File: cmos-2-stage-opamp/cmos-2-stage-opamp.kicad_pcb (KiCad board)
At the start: 2 copper layers, 39 x 34.5 mm, 35 parts, among them J1 Conn_01x05, Q1 DMN62DOU, Q2 DMN62DOU, Q3 DMN2004DMK-7, Q4 DMP2240UDM-7, Q5 DMN62DOU, Q8 DMP510DL, Q9 DMN62DOU

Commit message: cleanup: added annotations for tp + board images
DRC passed
Ready to submit to OSHPark
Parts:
- moved Q4 2.57 mm to (144.5, 61.8)
- renumbered TP1 to TP1VDD, TP2 to TP2Out, TP3 to TP3Bias, TP4 to TP4Bias, TP5 to TP5VSS, TP6 to TP6Tail, TP7 to TP7Mirror
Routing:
- net Net-(C1-Pad1): track 67.0 -> 70.9 mm
- net VDD: track 63.4 -> 66.9 mm
- net Net-(Q4A-DN): track 4.66 -> 8.11 mm
- net Net-(Q4B-SP): track 4.29 -> 7.31 mm
- net /mirror: track 25.6 -> 27.9 mm
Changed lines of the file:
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@@
 		)
 		(fp_text user "${REFERENCE}"
-			(at -4.445 4 360)
+			(at -4.445 4 0)
 			(layer "F.Fab")
 			(effects
@@
 		)
 		(fp_text user "${REFERENCE}"
-			(at 0 0 360)
+			(at 0 0 0)
 			(layer "F.Fab")
 			(effects
@@
 		(descr "SMD rectangular pad as test Point, square 1.5mm side length")
 		(tags "test point SMD pad rectangle square")
-		(property "Reference" "TP7"
+		(property "Reference" "TP7Mirror"
 			(at 0 -1.648 0)
 			(layer "F.SilkS")
@@
 	(footprint "Package_TO_SOT_SMD:SOT-363_SC-70-6_Handsoldering"
 		(layer "F.Cu")
-		(at 142.7 63.5875)
+		(at 144.52 61.77)
 		(descr "SOT-363, SC-70-6, Handsoldering")
 		(tags "SOT-363 SC-70-6 Handsoldering")
@@
 		(descr "SMD rectangular pad as test Point, square 1.5mm side length")
 		(tags "test point SMD pad rectangle square")
-		(property "Reference" "TP6"
-			(at 0 -1.648 0)
+		(property "Reference" "TP6Tail"
+			(at -0.15 1.91 0)
 			(layer "F.SilkS")
 			(effects
@@
 		(descr "SMD rectangular pad as test Point, square 1.5mm side length")
 		(tags "test point SMD pad rectangle square")
-		(property "Reference" "TP2"
+		(property "Reference" "TP2Out"
 			(at 0 1.648 0)
 			(layer "B.SilkS")
@@
 		(descr "SMD rectangular pad as test Point, square 1.5mm side length")
 		(tags "test point SMD pad rectangle square")
-		(property "Reference" "TP3"
-			(at 0 1.648 0)
+		(property "Reference" "TP3Bias"
+			(at -0.14 1.56 0)
 			(layer "B.SilkS")
 			(effects
@@
 		(descr "SMD rectangular pad as test Point, square 1.5mm side length")
 		(tags "test point SMD pad rectangle square")
-		(property "Reference" "TP1"
+		(property "Reference" "TP1VDD"
 			(at 0 1.648 0)
 			(layer "B.SilkS")
@@
 		(descr "SMD rectangular pad as test Point, square 1.5mm side length")
 		(tags "test point SMD pad rectangle square")
-		(property "Reference" "TP5"
+		(property "Reference" "TP5VSS"
 			(at -0.16 1.82 0)
 			(layer "B.SilkS")
 			(effects
 				(font
-					(size 1 1)
+					(size 0.8 0.8)
 					(thickness 0.15)
 				)
@@
 		(descr "SMD rectangular pad as test Point, square 1.5mm side length")
 		(tags "test point SMD pad rectangle square")
-		(property "Reference" "TP4"
-			(at 0 1.66 0)
+		(property "Reference" "TP4Bias"
+			(at 0.3 1.58 0)
 			(layer "B.SilkS")
 			(effects
 				(font
-					(size 1 1)
-					(thickness 0.15)
+					(size 0.65 0.65)
+					(thickness 0.125)
 				)
 				(justify mirror)
@@
 	)
 	(segment
-		(start 138.15 70.79)
-		(end 137.331151 71.608849)
+		(start 149.42 51.25)
+		(end 149.42 68.52)
 		(width 0.2)
 		(layer "F.Cu")
@@
 	)
 	(segment
-		(start 146.55 48.38)
-		(end 146.55 68.695685)
+		(start 131.253129 60.236871)
+		(end 134.913129 60.236871)
 		(width 0.2)
 		(layer "F.Cu")
@@
 	)
 	(segment
-		(start 144.225685 71.02)
-		(end 140.708529 71.02)
+		(start 137.37 57.78)
+		(end 137.21 57.62)
 		(width 0.2)
 		(layer "F.Cu")
@@
 	)
 	(segment
-		(start 131.253129 60.236871)
-		(end 134.913129 60.236871)
+		(start 146.92 71.02)
+		(end 140.708529 71.02)
 		(width 0.2)
 		(layer "F.Cu")
@@
 	)
 	(segment
-		(start 137.37 57.78)
-		(end 137.21 57.62)
-		(width 0.2)
-		(layer "F.Cu")
-		(net 2)
-	)
-	(segment
 		(start 137.331151 71.608849)
 		(end 137.331151 71.75)
@@
 	)
 	(segment
-		(start 140.708529 71.02)
-		(end 140.478529 70.79)
+		(start 146.55 48.38)
+		(end 149.42 51.25)
 		(width 0.2)
 		(layer "F.Cu")
@@
 	)
 	(segment
+		(start 149.42 68.52)
+		(end 146.92 71.02)
+		(width 0.2)
+		(layer "F.Cu")
+		(net 2)
+	)
+	(segment
+		(start 138.15 70.79)
+		(end 137.331151 71.608849)
+		(width 0.2)
+		(layer "F.Cu")
+		(net 2)
+	)
+	(segment
 		(start 129.04 59.35)
 		(end 130.59 60.9)
@@
 	)
 	(segment
-		(start 146.55 68.695685)
-		(end 144.225685 71.02)
+		(start 140.708529 71.02)
+		(end 140.478529 70.79)
 		(width 0.2)
 		(layer "F.Cu")
@@
 	)
 	(segment
+		(start 148.5 68.64)
+		(end 148.5 53.44)
+		(width 0.2)
+		(layer "F.Cu")
+		(net 3)
+	)
+	(segment
 		(start 141.7125 68.5325)
 		(end 141.2575 68.5325)
@@
 	)
 	(segment
-		(start 144.39 68.615)
-		(end 146.04 68.64)
+		(start 148.5 53.44)
+		(end 145.63 50.57)
 		(width 0.2)
 		(layer "F.Cu")
@@
 	)
 	(segment
-		(start 145.54 50.48)
-		(end 145.63 50.57)
+		(start 144.39 68.615)
+		(end 148.5 68.64)
 		(width 0.2)
 		(layer "F.Cu")
@@
 	)
 	(segment
-		(start 146.04 68.64)
-		(end 146.04 50.98)
+		(start 145.54 50.48)
+		(end 145.63 50.57)
 		(width 0.2)
 		(layer "F.Cu")
@@
 	)
 	(segment
-		(start 146.04 50.98)
-		(end 145.63 50.57)
-		(width 0.2)
-		(layer "F.Cu")
-		(net 3)
-	)
-	(segment
 		(start 141.7125 68.5325)
 		(end 144.3075 68.5325)
@@
 	)
 	(segment
+		(start 142.14 62.37)
+		(end 142.19 62.42)
+		(width 0.2)
+		(layer "F.Cu")
+		(net 11)
+	)
+	(segment
 		(start 138.91 68.58)
 		(end 140.83 66.66)
@@
 	)
 	(segment
-		(start 140.620001 62.9375)
-		(end 140.32 63.237501)
+		(start 125.46 67.878456)
+		(end 126.161544 68.58)
 		(width 0.2)
 		(layer "F.Cu")
@@
 	)
 	(segment
-		(start 141.37 62.9375)
-		(end 144.03 62.9375)
+		(start 141.971815 62.42)
+		(end 140.83 63.561815)
 		(width 0.2)
 		(layer "F.Cu")
@@
 	)
 	(segment
-		(start 140.83 64.7775)
-		(end 141.37 64.2375)
+		(start 142.440001 61.12)
+		(end 142.14 61.420001)
 		(width 0.2)
 		(layer "F.Cu")
@@
 	)
 	(segment
-		(start 141.37 62.9375)
-		(end 140.620001 62.9375)
+		(start 142.14 61.420001)
+		(end 142.14 62.37)
 		(width 0.2)
 		(layer "F.Cu")
@@
 	)
 	(segment
-		(start 125.46 67.878456)
-		(end 126.161544 68.58)
+		(start 140.83 63.561815)
+		(end 140.83 64.7775)
 		(width 0.2)
 		(layer "F.Cu")
@@
 	)
 	(segment
-		(start 140.32 63.237501)
-		(end 140.32 64.12)
+		(start 142.19 62.42)
+		(end 143.19 62.42)
+		(width 0.2)
+		(layer "F.Cu")
+		(net 11)
+	)
+	(segment
+		(start 142.19 62.42)
+		(end 141.971815 62.42)
 		(width 0.2)
 		(layer "F.Cu")
@@
 	)
 	(segment
-		(start 131.42 68.58)
-		(end 138.91 68.58)
+		(start 143.19 61.12)
+		(end 145.85 61.12)
 		(width 0.2)
 		(layer "F.Cu")
@@
 	)
 	(segment
-		(start 140.4375 64.2375)
-		(end 141.37 64.2375)
+		(start 131.42 68.58)
+		(end 138.91 68.58)
 		(width 0.2)
 		(layer "F.Cu")
@@
 	)
 	(segment
-		(start 140.32 64.12)
-		(end 140.4375 64.2375)
+		(start 143.19 61.12)
+		(end 142.440001 61.12)
 		(width 0.2)
 		(layer "F.Cu")
@@
 	)
 	(segment
-		(start 145.1725 64.2375)
-		(end 145.42 63.99)
+		(start 126.76 69.87)
+		(end 127.28 70.39)
 		(width 0.2)
 		(layer "F.Cu")
@@
 	)
 	(segment
-		(start 144.03 64.2375)
-		(end 145.1725 64.2375)
+		(start 145.43 63.98)
+		(end 145.44 63.98)
 		(width 0.2)
 		(layer "F.Cu")
@@
 	)
 	(segment
-		(start 126.76 69.87)
-		(end 127.28 70.39)
+		(start 145.85 62.42)
+		(end 145.85 63.57)
 		(width 0.2)
 		(layer "F.Cu")
@@
 	)
 	(segment
-		(start 145.43 63.98)
-		(end 145.44 63.98)
+		(start 145.42 63.99)
+		(end 145.43 63.98)
 		(width 0.2)
 		(layer "F.Cu")
@@
 	)
 	(segment
-		(start 145.42 63.99)
-		(end 145.43 63.98)
+		(start 145.85 63.57)
+		(end 145.44 63.98)
 		(width 0.2)
 		(layer "F.Cu")
@@
 	)
 	(segment
-		(start 142.42 63.887501)
-		(end 142.42 66)
+		(start 143.19 61.77)
+		(end 143.939999 61.77)
 		(width 0.2)
 		(layer "F.Cu")
@@
 	)
 	(segment
-		(start 142.119999 63.5875)
-		(end 142.42 63.887501)
+		(start 144.24 62.070001)
+		(end 144.24 62.688456)
+		(width 0.2)
+		(layer "F.Cu")
+		(net 15)
+	)
+	(segment
+		(start 144.24 62.688456)
+		(end 143.740956 63.1875)
+		(width 0.2)
+		(layer "F.Cu")
+		(net 15)
+	)
+	(segment
+		(start 142.42 63.74)
+		(end 142.42 66)
 		(width 0.2)
 		(layer "F.Cu")
@@
 	)
 	(segment
-		(start 141.37 63.5875)
-		(end 142.119999 63.5875)
+		(start 143.740956 63.1875)
+		(end 142.9725 63.1875)
 		(width 0.2)
 		(layer "F.Cu")
@@
 	)
 	(segment
+		(start 142.9725 63.1875)
+		(end 142.42 63.74)
+		(width 0.2)
+		(layer "F.Cu")
+		(net 15)
+	)
+	(segment
+		(start 143.939999 61.77)
+		(end 144.24 62.070001)
+		(width 0.2)
+		(layer "F.Cu")
+		(net 15)
+	)
+	(segment
+		(start 145.158456 61.77)
+		(end 144.78 62.148456)
+		(width 0.2)
+		(layer "F.Cu")
+		(net 16)
+	)
+	(segment
+		(start 144.78 63.61)
+		(end 144.0525 63.61)
+		(width 0.2)
+		(layer "F.Cu")
+		(net 16)
+	)
+	(segment
+		(start 144.0525 63.61)
+		(end 144.03 63.5875)
+		(width 0.2)
+		(layer "F.Cu")
+		(net 16)
+	)
+	(segment
+		(start 144.78 62.148456)
+		(end 144.78 63.61)
+		(width 0.2)
+		(layer "F.Cu")
+		(net 16)
+	)
+	(segment
 		(start 142.98 63.887501)
 		(end 142.98 65.38)
@@
 		(width 0.2)
 		(layer "F.Cu")
+		(net 16)
+	)
+	(segment
+		(start 145.85 61.77)
+		(end 145.158456 61.77)
+		(width 0.2)
+		(layer "F.Cu")

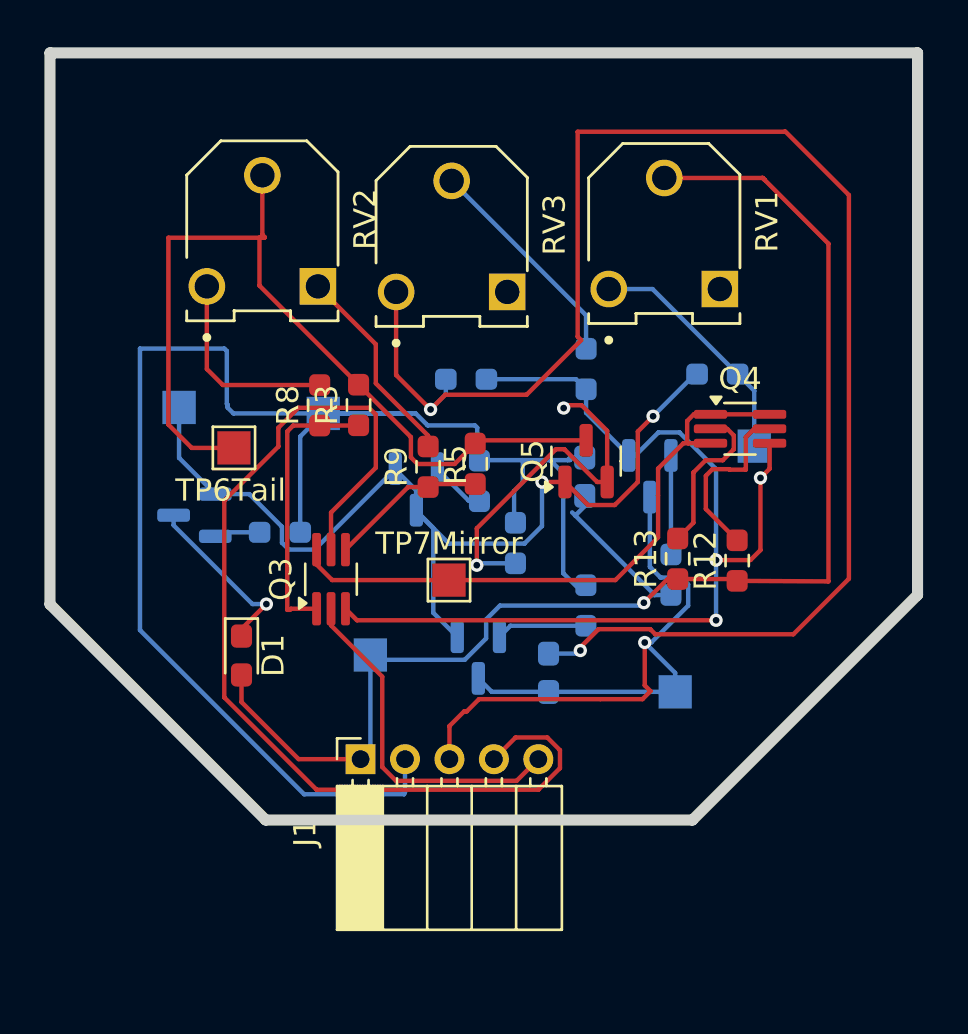
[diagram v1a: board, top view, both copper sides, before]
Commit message: final update on board
added senior design and date approved to chip using silkscreen.
added name of chip 2 stage cmos op-amp.
updated footprint of chip from 2.00 1*05 pin conn to 2.54 1*05 pin conn.
ran DRC and everything checks out perfectly.
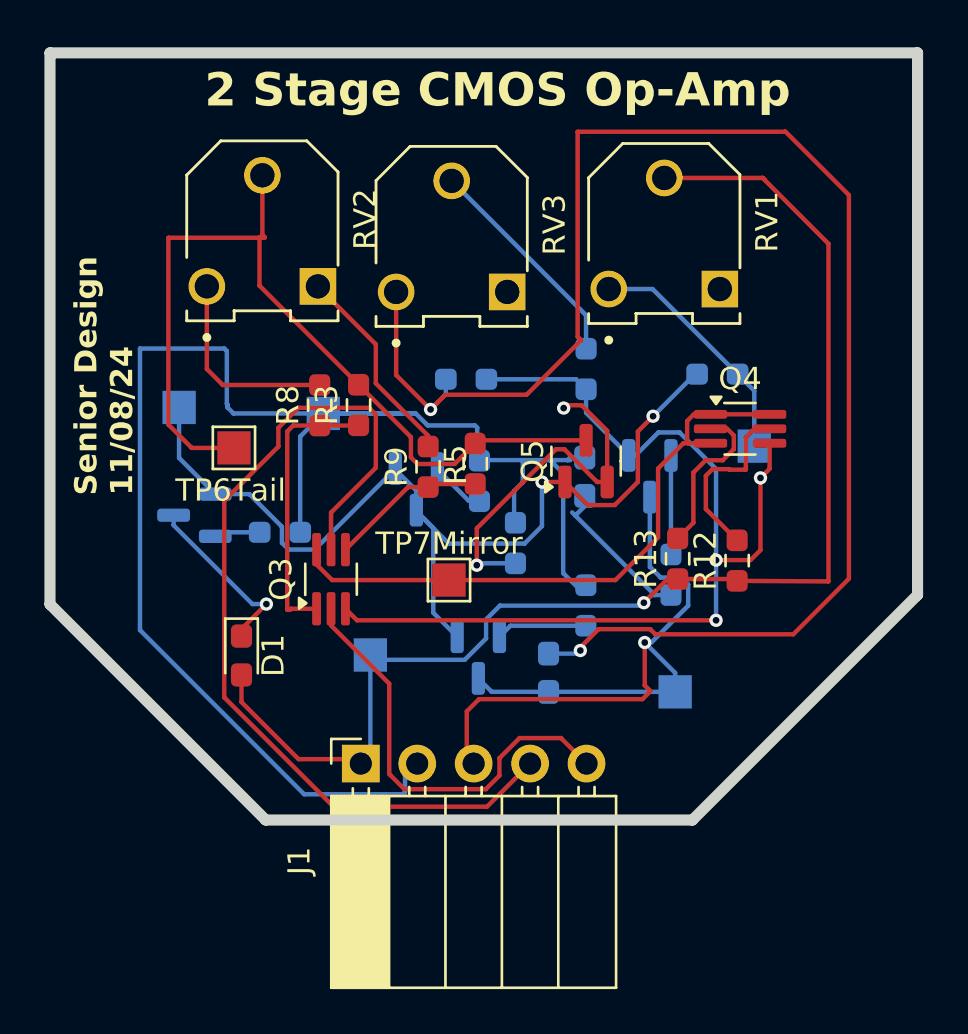
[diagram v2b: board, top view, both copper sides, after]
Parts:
- J1: footprint Connector_PinSocket_2.00mm:PinSocket_1x05_P2.00mm_Horizontal -> Connector_PinSocket_2.54mm:PinSocket_1x05_P2.54mm_Horizontal
- moved J1 0.20 mm to (127.5, 76.8)
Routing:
- net V+: track 46.6 -> 41.5 mm
- net V-: track 15.8 -> 19.6 mm
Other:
- board text added: "2 Stage CMOS Op-Amp"
- board text added: "Senior Design 11/08/24"

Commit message: update to names of rv1, rv2, rv3 of board
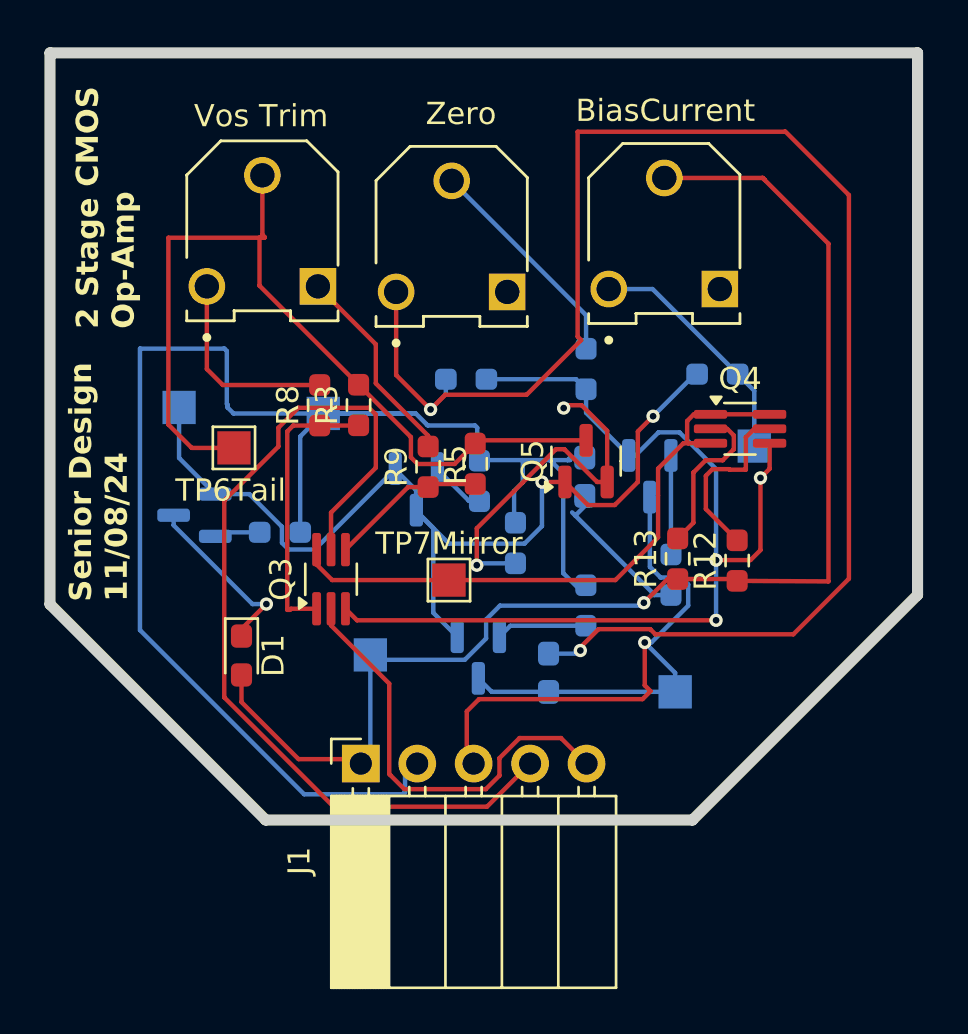
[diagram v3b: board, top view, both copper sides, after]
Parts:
- Vos Trim: renamed from RV2
- Zero : renamed from RV3
- renumbered RV1 to BiasCurrent
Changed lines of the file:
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@@
 		(layer "F.Cu")
 		(at 123.02 52.86 -90)
-		(property "Reference" "RV2"
-			(at -0.525 -4.625 90)
+		(property "Reference" "Vos Trim"
+			(at -5.17 0.06 180)
 			(layer "F.SilkS")
 			(effects
@@
 		(layer "F.Cu")
 		(at 131.54 53.11 -90)
-		(property "Reference" "RV3"
-			(at -0.525 -4.625 90)
+		(property "Reference" "Zero "
+			(at -5.52 -0.42 0)
 			(layer "F.SilkS")
 			(effects
@@
 		(layer "F.Cu")
 		(at 141.11 52.98 -90)
-		(property "Reference" "RV1"
-			(at -0.525 -4.625 90)
+		(property "Reference" "BiasCurrent"
+			(at -5.53 -0.05 360)
 			(layer "F.SilkS")
 			(effects
@@
 	)
 	(gr_text "Senior Design\n11/08/24\n"
-		(at 117.28 64.77 90)
+		(at 117.04 69.55 90)
 		(layer "F.SilkS")
 		(effects
@@
 		)
 	)
-	(gr_text "2 Stage CMOS Op-Amp"
-		(at 120.42 47.4 0)
+	(gr_text "2 Stage CMOS \nOp-Amp"
+		(at 117.35 57.27 90)
 		(layer "F.SilkS")
 		(effects
 			(font
-				(size 1.5 1.5)
-				(thickness 0.3)
+				(size 1 1)
+				(thickness 0.25)
 				(bold yes)
 			)
